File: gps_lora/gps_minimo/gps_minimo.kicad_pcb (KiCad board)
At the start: 2 copper layers, 30 parts, among them J1 USB_B, J2 BAT, J3 SWD, Q1 Q_PMOS_GSD, SW1 RST, U1 AP2114-3.3, U2 MCP73831-3-OT, U3 ATSAMD21E, U4 RFM95W-868S2

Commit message: add pcb gps vehicular and minimo
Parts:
- C7, D1, D3, D4, D5, J1, J2, J3, MODULE1, R3, R6, R7, SW1: moved to B.Cu
- moved U2 91.1 mm to (120.9, 96.6), turned to 180 degrees
- moved D1 89.3 mm to (113.7, 92.3), turned to 180 degrees
- moved J2 87.1 mm to (123.3, 106.0), turned to 90 degrees
- moved R1 87.0 mm to (115.5, 87.0), turned to 180 degrees
- moved R4 86.6 mm to (126.6, 95.9)
- moved D2 85.9 mm to (115.3, 84.6)
- moved J1 85.1 mm to (107.7, 89.7), turned to 90 degrees
- moved C5 85.1 mm to (115.5, 96.6), turned to 180 degrees
- moved C2 84.9 mm to (115.5, 94.0), turned to 180 degrees
- moved Q1 84.9 mm to (120.8, 86.0), turned to 90 degrees
- moved R3 81.3 mm to (118.6, 76.9), turned to 270 degrees
- moved C4 77.0 mm to (127.3, 86.3), turned to 270 degrees
- moved R2 77.0 mm to (120.8, 100.8)
- moved C1 75.2 mm to (115.5, 82.2), turned to 180 degrees
- moved R5 74.9 mm to (126.6, 98.3), turned to 180 degrees
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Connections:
- U3 pad 1: Net-(U3-Pad1) -> /microcontroller/LED_1
- U3 pad 15: Net-(U3-Pad15) -> /microcontroller/1PPS
- U3 pad 2: Net-(U3-Pad2) -> /microcontroller/LED_2
- U3 pad 3: Net-(U3-Pad3) -> V_DIV
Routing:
- net +3V3: track 0.00 -> 108.1 mm, vias 0 -> 3
- net /microcontroller/DIO0: track 0.00 -> 41.8 mm, vias 0 -> 2
- net +5V: track 0.00 -> 40.9 mm, vias 0 -> 2
- net D+: track 0.00 -> 35.3 mm, vias 0 -> 1
- net D-: track 0.00 -> 34.9 mm, vias 0 -> 1
- net /microcontroller/DIO1: track 0.00 -> 30.3 mm
- net +BATT: track 0.00 -> 28.5 mm
- net /microcontroller/DIO2: track 0.00 -> 27.1 mm
- net /microcontroller/LED_2: track 0.00 -> 26.8 mm, vias 0 -> 1
- net Net-(R3-Pad2): track 0.00 -> 25.5 mm, vias 0 -> 3
- net /microcontroller/LED_1: track 0.00 -> 24.9 mm, vias 0 -> 1
- net /microcontroller/RST_SAMD: track 0.00 -> 24.4 mm, vias 0 -> 1
- net /microcontroller/1PPS: track 0.00 -> 22.8 mm, vias 0 -> 1
- net GND: track 0.00 -> 19.9 mm, vias 0 -> 18
- net V_DIV: track 0.00 -> 14.3 mm
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- added copper zone on B.Cu, net GND
- added copper zone on F.Cu, net GND
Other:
- board outline added: 70.9 x 42.6 mm
- net class Default: trace_width 0.25 -> 0.3
- net class Source added: clearance 0.2, trace_width 0.5, via_dia 0.9, via_drill 0.45
- rule trace_min: 0.2 -> 0.3
- board text added: "+"
- board text added: "-"
- board text added: "1"

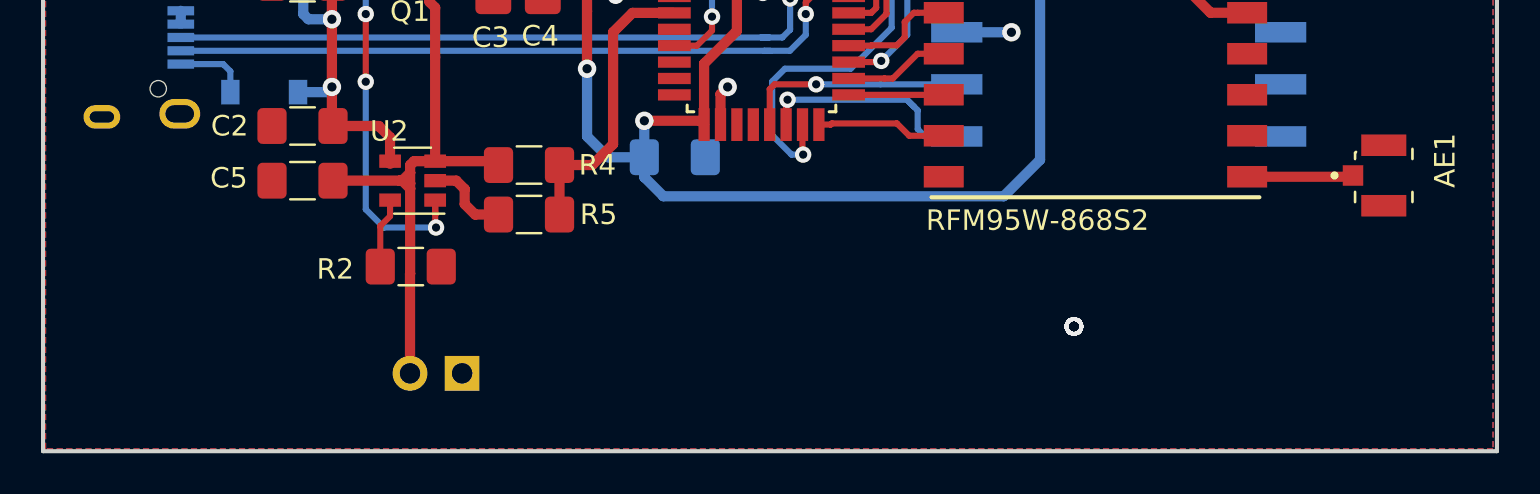
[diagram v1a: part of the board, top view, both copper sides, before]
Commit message: add logos gps minimo
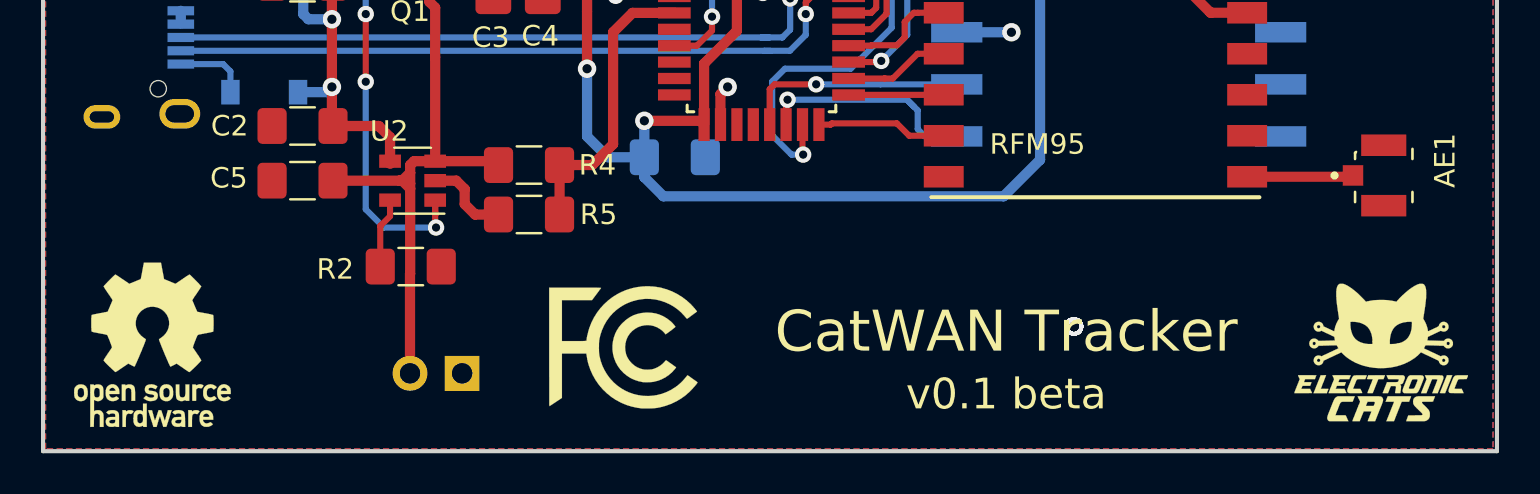
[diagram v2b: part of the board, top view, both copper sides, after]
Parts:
- added G***: LOGO, Aesthetics:electronic_cats_logo_8x6, F.Cu at (168.1, 105.0)
- added G***: LOGO, Aesthetics:electronic_cats_logo_8x6, B.Cu at (168.1, 105.2)
- added REF***: FCC-Logo_7.3x6mm_SilkScreen, Symbols:FCC-Logo_7.3x6mm_SilkScreen, F.Cu at (131.2, 104.8)
- added REF***: OSHW-Logo_7.5x8mm_SilkScreen, Symbols:OSHW-Logo_7.5x8mm_SilkScreen, F.Cu at (108.2, 104.6)
- added REF***: FCC-Logo_7.3x6mm_SilkScreen, Symbols:FCC-Logo_7.3x6mm_SilkScreen, B.Cu at (130.8, 104.9)
- added REF***: OSHW-Logo_7.5x8mm_SilkScreen, Symbols:OSHW-Logo_7.5x8mm_SilkScreen, B.Cu at (108.2, 104.8)
- U4: value RFM95W-868S2 -> RFM95
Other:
- board text added: "CatWAN Tracker"
- board text added: "v0.1 beta"

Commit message: Round off the corners and change screem  printing  gps_minimo
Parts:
- moved G*** 3.01 mm to (165.1, 105.2)
- moved G*** 2.93 mm to (165.2, 105.2)
- moved REF*** 2.08 mm to (110.3, 104.7)
- moved REF*** 2.03 mm to (110.2, 104.7)
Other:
- board size 70.9 x 42.6 mm -> 71 x 42.7 mm
- board text added: "3.3V"
- board text added: "GND"
- board text added: "SWCLK"
- board text added: "SWDIO"
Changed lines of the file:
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@@
-(kicad_pcb (version 20171130) (host pcbnew "(5.0.1-3-g963ef8bb5)")
+(kicad_pcb (version 20171130) (host pcbnew "(5.1.0)-1")
   (general
     (thickness 1.6)
-    (drawings 41)
+    (drawings 47)
     (tracks 321)
     (zones 0)
@@
     (zone_45_only no)
     (trace_min 0.3)
-    (segment_width 0.2)
-    (edge_width 0.15)
     (via_size 0.8)
     (via_drill 0.4)
@@
     (uvia_min_size 0.2)
     (uvia_min_drill 0.1)
+    (edge_width 0.15)
+    (segment_width 0.2)
     (pcb_text_width 0.3)
     (pcb_text_size 1.5 1.5)
@@
     (uvia_dia 0.3)
     (uvia_drill 0.1)
-    (diff_pair_gap 0.25)
     (diff_pair_width 0.3)
+    (diff_pair_gap 0.25)
     (add_net /microcontroller/1PPS)
     (add_net /microcontroller/DIO0)
@@
     (uvia_dia 0.3)
     (uvia_drill 0.1)
-    (diff_pair_gap 0.25)
     (diff_pair_width 0.3)
+    (diff_pair_gap 0.25)
     (add_net +3V3)
     (add_net +5V)
@@
     (tags "QFP 0.8")
     (attr smd)
-    (fp_text reference U3 (at -4.445 -6.05) (layer F.SilkS)
+    (fp_text reference U3 (at -4.532 -4.512) (layer F.SilkS)
       (effects (font (size 1 1) (thickness 0.15)))
     )
@@
     (at 168.275 96.393 270)
     (attr smd)
-    (fp_text reference AE1 (at -0.73118 -2.98984 270) (layer F.SilkS)
+    (fp_text reference AE1 (at -3.393 -0.035) (layer F.SilkS)
       (effects (font (size 1 1) (thickness 0.15)))
     )
@@
     (tags "capacitor handsolder")
     (attr smd)
-    (fp_text reference C7 (at 3.429 0 -90) (layer B.SilkS)
+    (fp_text reference C7 (at 0.0255 -1.964) (layer B.SilkS)
       (effects (font (size 1 1) (thickness 0.15)) (justify mirror))
     )
@@
       (effects (font (size 1 1) (thickness 0.15)) (justify mirror))
     )
-    (fp_text value USB_B (at 1.905 3.81 90) (layer B.SilkS)
+    (fp_text value USB_B (at 5.932 -0.026 180) (layer B.SilkS)
       (effects (font (size 1 1) (thickness 0.15)) (justify mirror))
     )
@@
       (effects (font (size 1 1) (thickness 0.15)))
     )
-    (fp_text value RFM95 (at -2.828 5.413) (layer F.SilkS)
+    (fp_text value RFM95 (at -6.462 9.534) (layer F.SilkS)
       (effects (font (size 1 1) (thickness 0.15)))
     )
@@
       (effects (font (size 1 1) (thickness 0.05)) (justify mirror))
     )
-    (fp_text value L80-M39 (at -3.276 -9.056 180) (layer B.SilkS)
+    (fp_text value L80-M39 (at -4.653 9.218 180) (layer B.SilkS)
       (effects (font (size 1 1) (thickness 0.05)) (justify mirror))
     )
@@
     (tags SOD-123)
     (attr smd)
-    (fp_text reference D2 (at 0 -2) (layer F.SilkS)
+    (fp_text reference D2 (at -3.406 -0.042) (layer F.SilkS)
       (effects (font (size 1 1) (thickness 0.15)))
     )
@@
   )
   (module Aesthetics:electronic_cats_logo_8x6 (layer F.Cu)
-    (at 168.148 105.029)
+    (at 165.23 105.24)
     (fp_text reference G*** (at 0 0) (layer F.SilkS) hide
       (effects (font (size 1.524 1.524) (thickness 0.3)))
@@
   )
   (module Aesthetics:electronic_cats_logo_8x6 (layer B.Cu)
-    (at 168.148 105.156 180)
+    (at 165.14 105.24 180)
     (fp_text reference G*** (at 0 0 180) (layer B.SilkS) hide
       (effects (font (size 1.524 1.524) (thickness 0.3)) (justify mirror))
@@
   )
   (module Symbols:OSHW-Logo_7.5x8mm_SilkScreen (layer F.Cu)
-    (at 108.204 104.648)
+    (at 110.23 104.69)
     (descr "Open Source Hardware Logo")
     (tags "Logo OSHW")
@@
   )
   (module Symbols:OSHW-Logo_7.5x8mm_SilkScreen (layer B.Cu)
-    (at 108.204 104.775 180)
+    (at 110.28 104.69 180)
     (descr "Open Source Hardware Logo")
     (tags "Logo OSHW")
@@
       (xy 0.500964 3.601424)) (layer B.SilkS) (width 0.01))
   )
-  (gr_text "CatWAN Tracker" (at 149.733 104.013) (layer B.SilkS)
+  (gr_text "GND\n\n" (at 142.59 71.14 90) (layer F.SilkS)
+    (effects (font (size 1 1) (thickness 0.15)))
+  )
+  (gr_text "SWCLK\n" (at 139.19 70.29 90) (layer F.SilkS)
+    (effects (font (size 1 1) (thickness 0.15)))
+  )
+  (gr_text "SWDIO\n" (at 136.64 70.38 90) (layer F.SilkS)
+    (effects (font (size 1 1) (thickness 0.15)))
+  )
+  (gr_text 3.3V (at 134.14 70.99 90) (layer F.SilkS)
+    (effects (font (size 1 1) (thickness 0.15)))
+  )
+  (gr_arc (start 169.03 105.07) (end 169.03 109.85) (angle -90) (layer Edge.Cuts) (width 0.2))
+  (gr_arc (start 107.64 105.05) (end 102.86 105.05) (angle -90) (layer Edge.Cuts) (width 0.2))
+  (gr_text "CatWAN Tracker" (at 148.41 104.13) (layer B.SilkS)
     (effects (font (size 2 2) (thickness 0.3)) (justify mirror))
   )
-  (gr_text "v0.1 beta" (at 149.86 107.061) (layer F.SilkS)
+  (gr_text "v0.1 beta" (at 147.9 107.13) (layer F.SilkS)
     (effects (font (size 1.5 1.5) (thickness 0.3)))
   )
-  (gr_text "CatWAN Tracker" (at 149.86 104.013) (layer F.SilkS)
+  (gr_text "CatWAN Tracker" (at 148.15 103.96) (layer F.SilkS)
     (effects (font (size 2 2) (thickness 0.3)))
   )
@@
   )
   (gr_line (start 163.173 77.8452) (end 163.158 77.8328) (layer Edge.Cuts) (width 0.2))
-  (gr_line (start 173.797 109.8435) (end 173.797 77.8617) (layer Edge.Cuts) (width 0.2))
+  (gr_line (start 173.81 105.07) (end 173.797 77.8617) (layer Edge.Cuts) (width 0.2))
   (gr_line (start 113.501 77.8452) (end 113.483 77.8545) (layer Edge.Cuts) (width 0.2))
   (gr_line (start 113.445 77.8622) (end 113.44 77.8617) (layer Edge.Cuts) (width 0.2))
@@
   (gr_line (start 163.145 77.8175) (end 163.136 77.8002) (layer Edge.Cuts) (width 0.2))
   (gr_line (start 163.129 67.1937) (end 113.545 67.1937) (layer Edge.Cuts) (width 0.2))
-  (gr_line (start 102.877 109.8435) (end 173.797 109.8435) (layer Edge.Cuts) (width 0.2))
-  (gr_line (start 102.877 77.8617) (end 102.877 109.8435) (layer Edge.Cuts) (width 0.2))
+  (gr_line (start 107.64 109.83) (end 169.03 109.85) (layer Edge.Cuts) (width 0.2))
+  (gr_line (start 102.877 77.8617) (end 102.86 105.05) (layer Edge.Cuts) (width 0.2))
   (gr_line (start 173.797 77.8617) (end 163.234 77.8617) (layer Edge.Cuts) (width 0.2))
   (gr_line (start 113.516 77.8328) (end 113.501 77.8452) (layer Edge.Cuts) (width 0.2))
@@
   (segment (start 120.777 84.979) (end 120.777 82.208) (width 0.5) (layer F.Cu) (net 3))
   (segment (start 117.021 82.169) (end 120.788 82.169) (width 0.5) (layer F.Cu) (net 3))
-  (segment (start 116.078 82.169) (end 117.021 82.169) (width 0.5) (layer F.Cu) (net 3) (status 1000000))
-  (segment (start 113.794 84.582) (end 115.189 84.582) (width 0.5) (layer F.Cu) (net 3) (status 1000000))
-  (segment (start 115.57 82.677) (end 116.078 82.169) (width 0.5) (layer F.Cu) (net 3) (status 1000000))
-  (segment (start 115.189 84.582) (end 115.57 84.201) (width 0.5) (layer F.Cu) (net 3) (status 1000000))
-  (segment (start 115.57 84.201) (end 115.57 82.677) (width 0.5) (layer F.Cu) (net 3) (status 1000000))
+  (segment (start 116.078 82.169) (end 117.021 82.169) (width 0.5) (layer F.Cu) (net 3))
+  (segment (start 113.794 84.582) (end 115.189 84.582) (width 0.5) (layer F.Cu) (net 3))
+  (segment (start 115.57 82.677) (end 116.078 82.169) (width 0.5) (layer F.Cu) (net 3))
+  (segment (start 115.189 84.582) (end 115.57 84.201) (width 0.5) (layer F.Cu) (net 3))
+  (segment (start 115.57 84.201) (end 115.57 82.677) (width 0.5) (layer F.Cu) (net 3))
   (segment (start 119.738 95.758) (end 119.804 95.824) (width 0.5) (layer F.Cu) (net 4))
   (segment (start 119.804 94.531) (end 119.804 95.697) (width 0.5) (layer F.Cu) (net 4))
@@
   (segment (start 116.967 92.075) (end 116.967 88.773) (width 0.5) (layer F.Cu) (net 4))
   (segment (start 116.967 88.773) (end 116.967 87.049) (width 0.5) (layer F.Cu) (net 4))
-  (segment (start 117.021 84.655) (end 117.094 84.582) (width 0.5) (layer F.Cu) (net 4) (status 1000000))
-  (segment (start 117.021 86.995) (end 117.021 84.655) (width 0.5) (layer F.Cu) (net 4) (status 1000000))
+  (segment (start 117.021 84.655) (end 117.094 84.582) (width 0.5) (layer F.Cu) (net 4))
+  (segment (start 117.021 86.995) (end 117.021 84.655) (width 0.5) (layer F.Cu) (net 4))
   (segment (start 120.802 79.883) (end 122.302 79.883) (width 0.5) (layer F.Cu) (net 5))
   (segment (start 124.841 84.836) (end 124.841 84.0235) (width 0.5) (layer F.Cu) (net 5))
@@
   (segment (start 143.002 80.899) (end 143.002 84.836) (width 0.3) (layer F.Cu) (net 43))
   (segment (start 144.018 79.883) (end 143.002 80.899) (width 0.3) (layer F.Cu) (net 43))
-  (zone (net 1) (net_name GND) (layer F.Cu) (hatch edge 0.508)
+  (zone (net 1) (net_name GND) (layer B.Cu) (hatch edge 0.508)
     (connect_pads (clearance 0.508))
     (min_thickness 0.254)
@@
     (polygon
       (pts
-        (xy 173.609 77.978) (xy 173.609 109.728) (xy 102.997 109.728) (xy 102.997 77.978) (xy 113.665 77.978)
-        (xy 113.665 67.31) (xy 162.941 67.31) (xy 162.941 77.978)
+        (xy 173.6 78.01) (xy 173.61 105.81) (xy 173.39 106.71) (xy 172.89 107.6) (xy 171.79 108.82)
+        (xy 170.91 109.3) (xy 169.98 109.59) (xy 169.47 109.7) (xy 107.2 109.7) (xy 106.3 109.5)
+        (xy 105.4 109.11) (xy 104.79 108.71) (xy 104.3 108.29) (xy 103.61 107.3) (xy 103.1 106)
+        (xy 102.99 105.3) (xy 103 104.5) (xy 103 78) (xy 113.6 78) (xy 113.65 67.3)
+        (xy 163.02 67.3) (xy 163 77.99) (xy 173.6 78)
       )
     )
   )
-  (zone (net 1) (net_name GND) (layer B.Cu) (hatch edge 0.508)
+  (zone (net 1) (net_name GND) (layer F.Cu) (hatch edge 0.508)
     (connect_pads (clearance 0.508))
     (min_thickness 0.254)
@@
     (polygon
       (pts
-        (xy 162.941 67.31) (xy 162.941 77.978) (xy 173.609 77.978) (xy 173.609 109.728) (xy 102.997 109.728)
-        (xy 102.997 77.978) (xy 113.665 77.978) (xy 113.665 67.31)
+        (xy 103 78.01) (xy 102.99 105.81) (xy 103.21 106.71) (xy 103.71 107.6) (xy 104.81 108.82)
+        (xy 105.69 109.3) (xy 106.62 109.59) (xy 107.13 109.7) (xy 169.4 109.7) (xy 170.3 109.5)
+        (xy 171.2 109.11) (xy 171.81 108.71) (xy 172.3 108.29) (xy 172.99 107.3) (xy 173.5 106)
+        (xy 173.61 105.3) (xy 173.6 104.5) (xy 173.6 78) (xy 163 78) (xy 162.95 67.3)
+        (xy 113.58 67.3) (xy 113.6 77.99) (xy 103 78)
       )
     )
